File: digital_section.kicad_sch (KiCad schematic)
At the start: 3 parts, among them U3 MCP3561RT-E_ST, U5 ISO7762FDW, U8 BluePill

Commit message: Added temperature, ref trimming and range selection resisitors.
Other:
- moved on the sheet: U5
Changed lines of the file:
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@@
 	(wire
 		(pts
-			(xy 259.08 105.41) (xy 259.08 107.95)
+			(xy 186.69 119.38) (xy 186.69 121.92)
 		)
 		(stroke
@@
 	(wire
 		(pts
-			(xy 259.08 143.51) (xy 259.08 140.97)
+			(xy 186.69 157.48) (xy 186.69 154.94)
 		)
 		(stroke
@@
 	(symbol
 		(lib_id "power:GND")
-		(at 259.08 143.51 0)
+		(at 186.69 157.48 0)
 		(unit 1)
 		(exclude_from_sim no)
@@
 		(fields_autoplaced yes)
 		(property "Reference" "#PWR010"
-			(at 259.08 149.86 0)
+			(at 186.69 163.83 0)
 			(effects
 				(font
@@
 		)
 		(property "Value" "GND"
-			(at 259.08 148.59 0)
+			(at 186.69 162.56 0)
 			(effects
 				(font
@@
 		)
 		(property "Footprint" ""
-			(at 259.08 143.51 0)
+			(at 186.69 157.48 0)
 			(effects
 				(font
@@
 		)
 		(property "Datasheet" ""
-			(at 259.08 143.51 0)
+			(at 186.69 157.48 0)
 			(effects
 				(font
@@
 		)
 		(property "Description" "Power symbol creates a global label with name \"GND\" , ground"
-			(at 259.08 143.51 0)
+			(at 186.69 157.48 0)
 			(effects
 				(font
@@
 	(symbol
 		(lib_id "Isolator:ISO7762FDW")
-		(at 264.16 125.73 0)
+		(at 191.77 139.7 0)
 		(mirror y)
 		(unit 1)
@@
 		(dnp no)
 		(property "Reference" "U5"
-			(at 272.542 110.998 0)
+			(at 200.152 124.968 0)
 			(effects
 				(font
@@
 		)
 		(property "Value" "ISO7762FDW"
-			(at 272.542 113.538 0)
+			(at 200.152 127.508 0)
 			(effects
 				(font
@@
 		)
 		(property "Footprint" "Package_SO:SOIC-16W_7.5x10.3mm_P1.27mm"
-			(at 258.445 139.7 0)
+			(at 186.055 153.67 0)
 			(effects
 				(font
@@
 		)
 		(property "Datasheet" "https://www.ti.com/lit/ds/symlink/iso7763.pdf?ts=1596905577895"
-			(at 254 128.27 0)
+			(at 181.61 142.24 0)
 			(effects
 				(font
@@
 		)
 		(property "Description" "Default low, High-speed, robust EMC, reinforced, six-channel, digital, isolator, SOIC-16"
-			(at 264.16 125.73 0)
+			(at 191.77 139.7 0)
 			(effects
 				(font
@@
 	(symbol
 		(lib_id "power:+3.3V")
-		(at 259.08 105.41 0)
+		(at 186.69 119.38 0)
 		(mirror y)
 		(unit 1)
@@
 		(fields_autoplaced yes)
 		(property "Reference" "#PWR09"
-			(at 259.08 109.22 0)
+			(at 186.69 123.19 0)
 			(effects
 				(font
@@
 		)
 		(property "Value" "+3.3V"
-			(at 259.08 100.33 0)
+			(at 186.69 114.3 0)
 			(effects
 				(font
@@
 		)
 		(property "Footprint" ""
-			(at 259.08 105.41 0)
+			(at 186.69 119.38 0)
 			(effects
 				(font
@@
 		)
 		(property "Datasheet" ""
-			(at 259.08 105.41 0)
+			(at 186.69 119.38 0)
 			(effects
 				(font
@@
 		)
 		(property "Description" "Power symbol creates a global label with name \"+3.3V\""
-			(at 259.08 105.41 0)
-			(effects
-				(font
+			(at 186.69 119.38 0)
+			(effects
+				(font

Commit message: on MCU
on MCU
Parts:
- added TP1, TP10, TP11, TP2, TP3, TP4, TP5, TP6, TP7, TP8, TP9: TestPoint, TestPoint:TestPoint_Pad_D3.0mm, symbol Connector:TestPoint
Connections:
- net +3.3V: now also U8.38 (3V3)
- net TX: now reaches U5.11 (INE)
- net TX: now also U8.6 (PA9)
- net RX: now reaches U5.12 (OUTD)
- net RX: now also U8.7 (PA10)
- net at U8.1 (PB12): now also TP1.1
- net at U8.14 (PB6): now also TP8.1
- net at U8.15 (PB7): now also TP9.1
- net at U8.16 (PB8): now also TP10.1
- net at U8.17 (PB9): now also TP11.1
- net at U8.2 (PB13): now also TP2.1
- net at U8.3 (PB14): now also TP3.1
- net SCLK: now reaches U3.14 (SCK), U8.30 (PA5)
- net MISO: now reaches U3.16 (SDO), U8.31 (PA6)
- net MOSI: now reaches U3.15 (SDI), U8.32 (PA7)
- net at U8.4 (PB15): now also TP4.1
- net at U8.5 (PA8): now also TP5.1
- net at U8.8 (PA11): now also TP6.1
- net at U8.9 (PA12): now also TP7.1
- net ~{CS} renamed CS
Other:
- moved on the sheet: U3

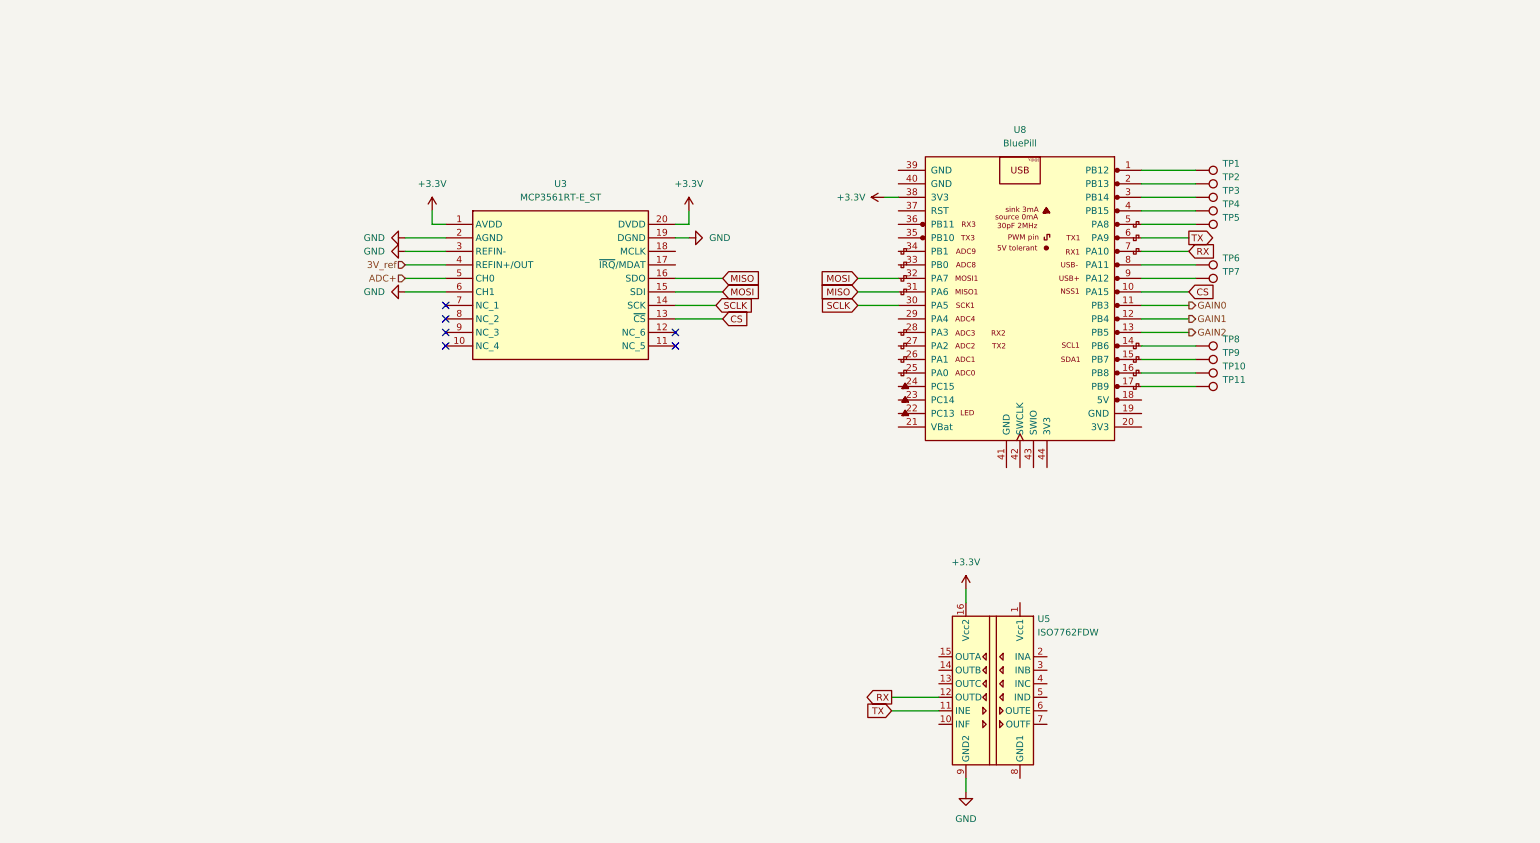
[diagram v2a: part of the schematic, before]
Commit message: Bootstraped input buffer.
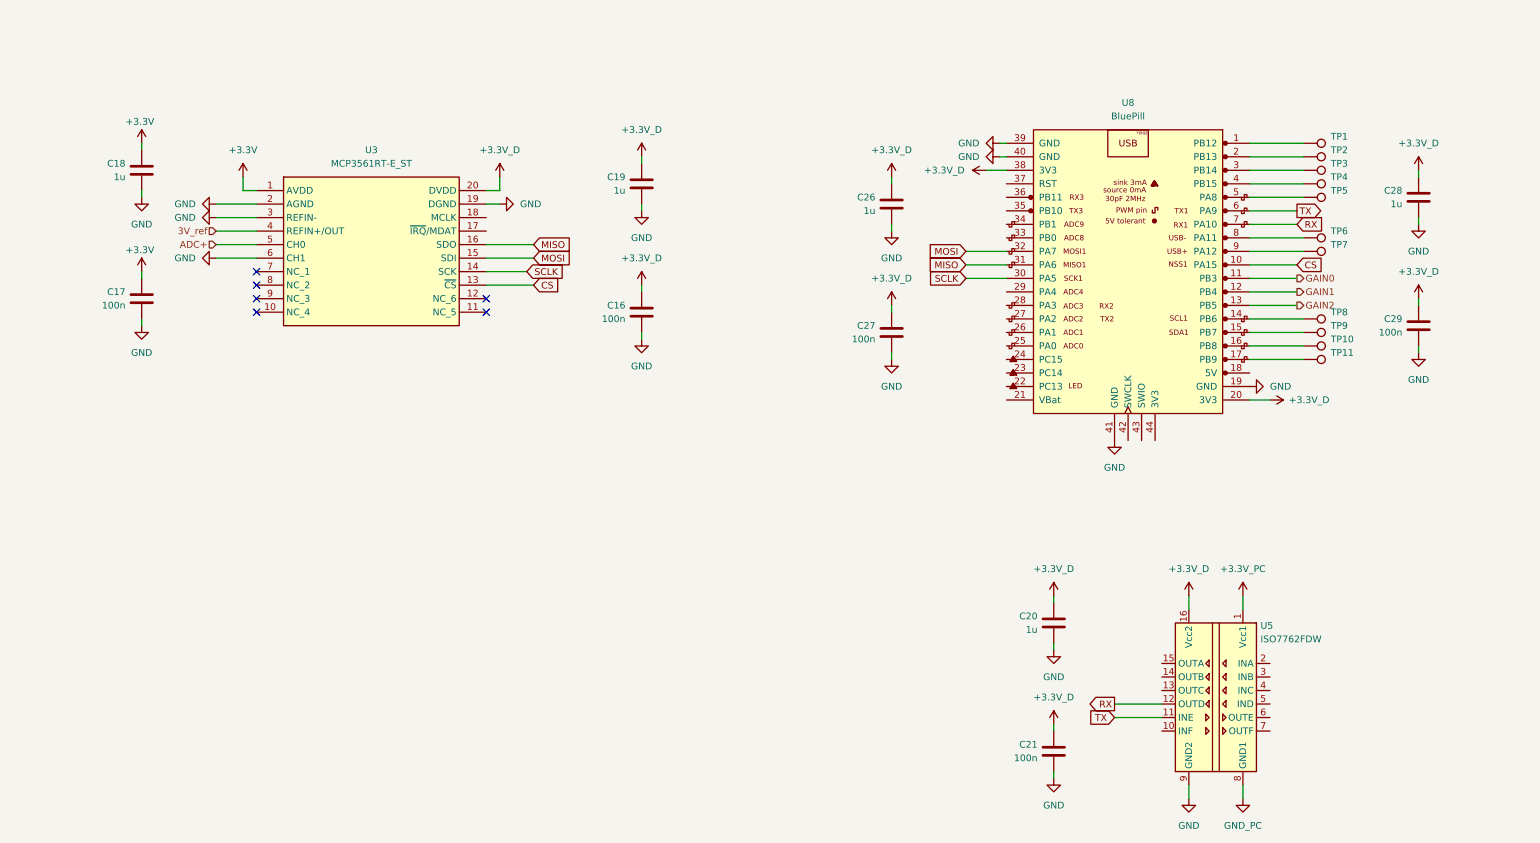
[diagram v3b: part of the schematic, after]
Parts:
- added C16, C17, C21, C27, C29: 100n, Capacitor_SMD:C_0603_1608Metric_Pad1.08x0.95mm_HandSolder, symbol Device:C
- added C18, C19, C20, C26, C28: 1u, Capacitor_SMD:C_0603_1608Metric_Pad1.08x0.95mm_HandSolder, symbol Device:C
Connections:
- net +3.3V: now also C17.2, C18.2; no longer U3.20 (DVDD), U5.16 (Vcc2), U8.38 (3V3)
- net GND: now also U8.19 (GND), U8.39 (GND), U8.40 (GND), U8.41 (GND), C16.1, C17.1, C18.1, C19.1, C20.1, C21.1, C26.1, C27.1, C28.1, C29.1
- net +3.3V_PC: now reaches U5.1 (Vcc1)
- net GND_PC: now reaches U5.8 (GND1)
- net +3.3V_D: now reaches U8.20 (3V3)
- net +3.3V_D: now also U3.20 (DVDD), U5.16 (Vcc2), U8.38 (3V3), C16.2, C19.2, C20.2, C21.2, C26.2, C27.2, C28.2, C29.2
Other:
- moved on the sheet: TP1, TP10, TP11, TP2, TP3, TP4, TP5, TP6, TP7, TP8, TP9, U3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
